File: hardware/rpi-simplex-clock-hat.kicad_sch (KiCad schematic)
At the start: 19 parts, among them J1 TBP01R1-508-04BE, J2 Barrel_Jack_Switch, J3 GPIO, U1 LAA120, U2 CAT24C256

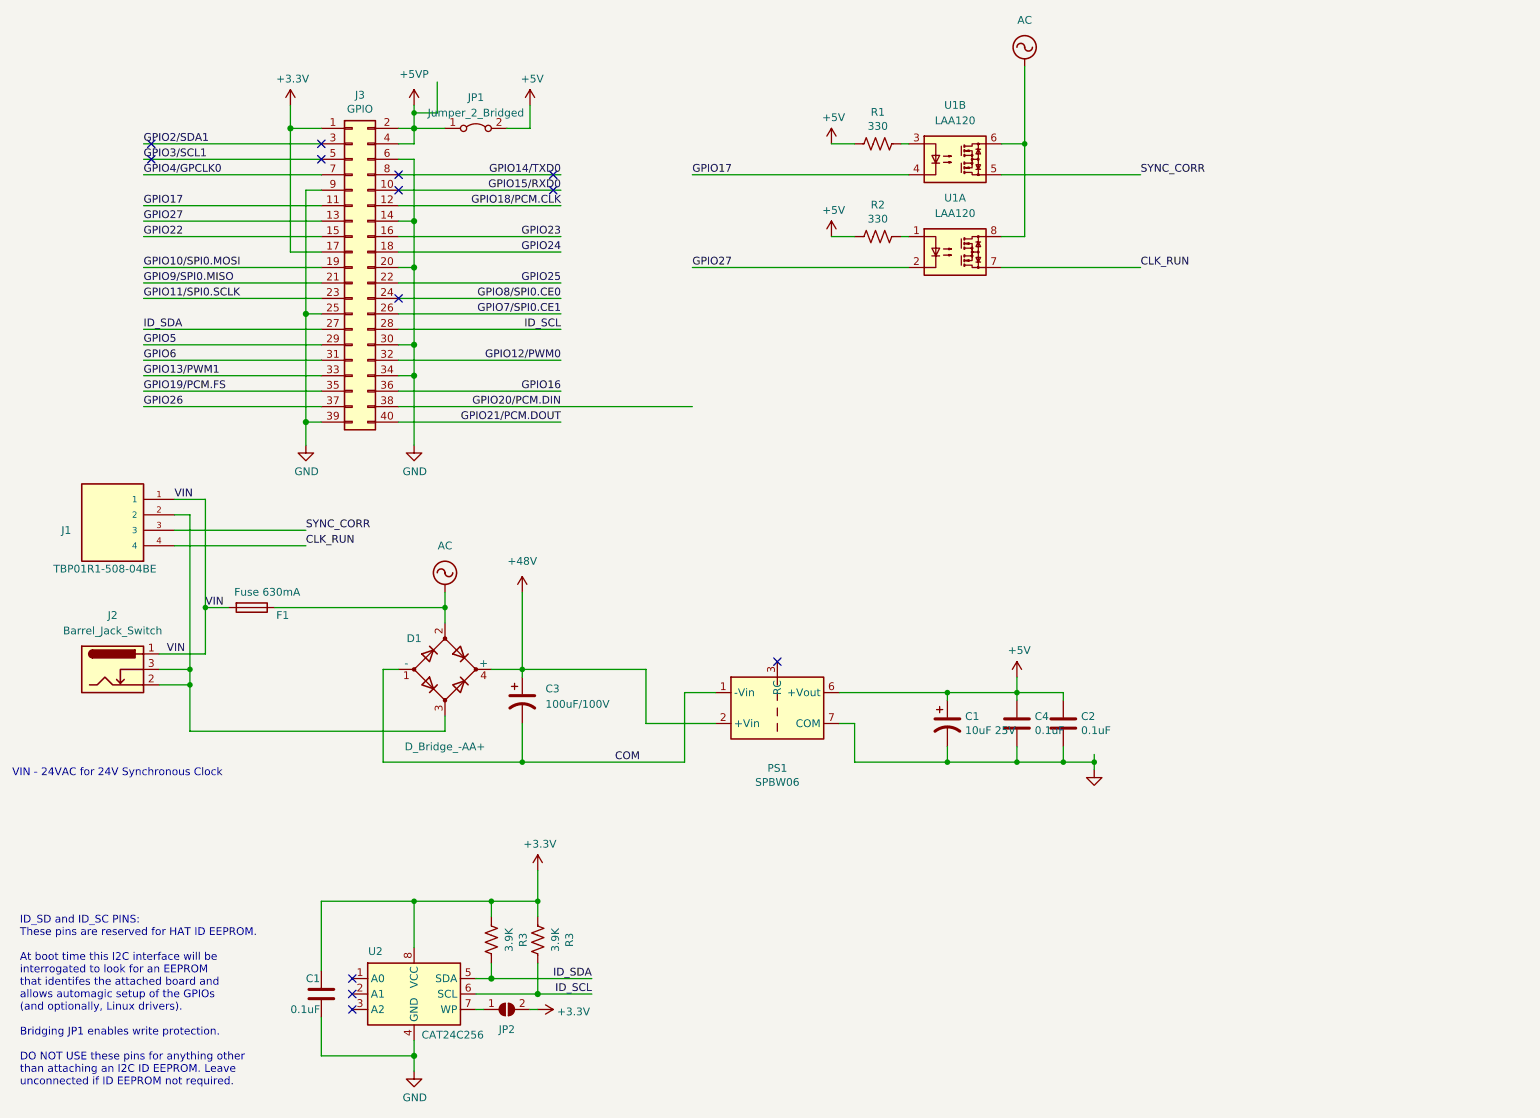
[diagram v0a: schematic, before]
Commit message: Rev 1: Fix minor issues in Rev 0.
1. Turn SSRs on with logic 1 to GPIO outputs.  This is needed so that
   the SSRs don't become enabled when the GPIO17 and GPIO27 are set to
   outputs.  These GPIOs are pulled low.

2. Add alternate footprint location (J4) for AC input barrel jack.

3. Add additional mounting holes for Raspberry Pi Zero / Zero 2 W.

4. Correct pinout for the bridge rectifier D1.
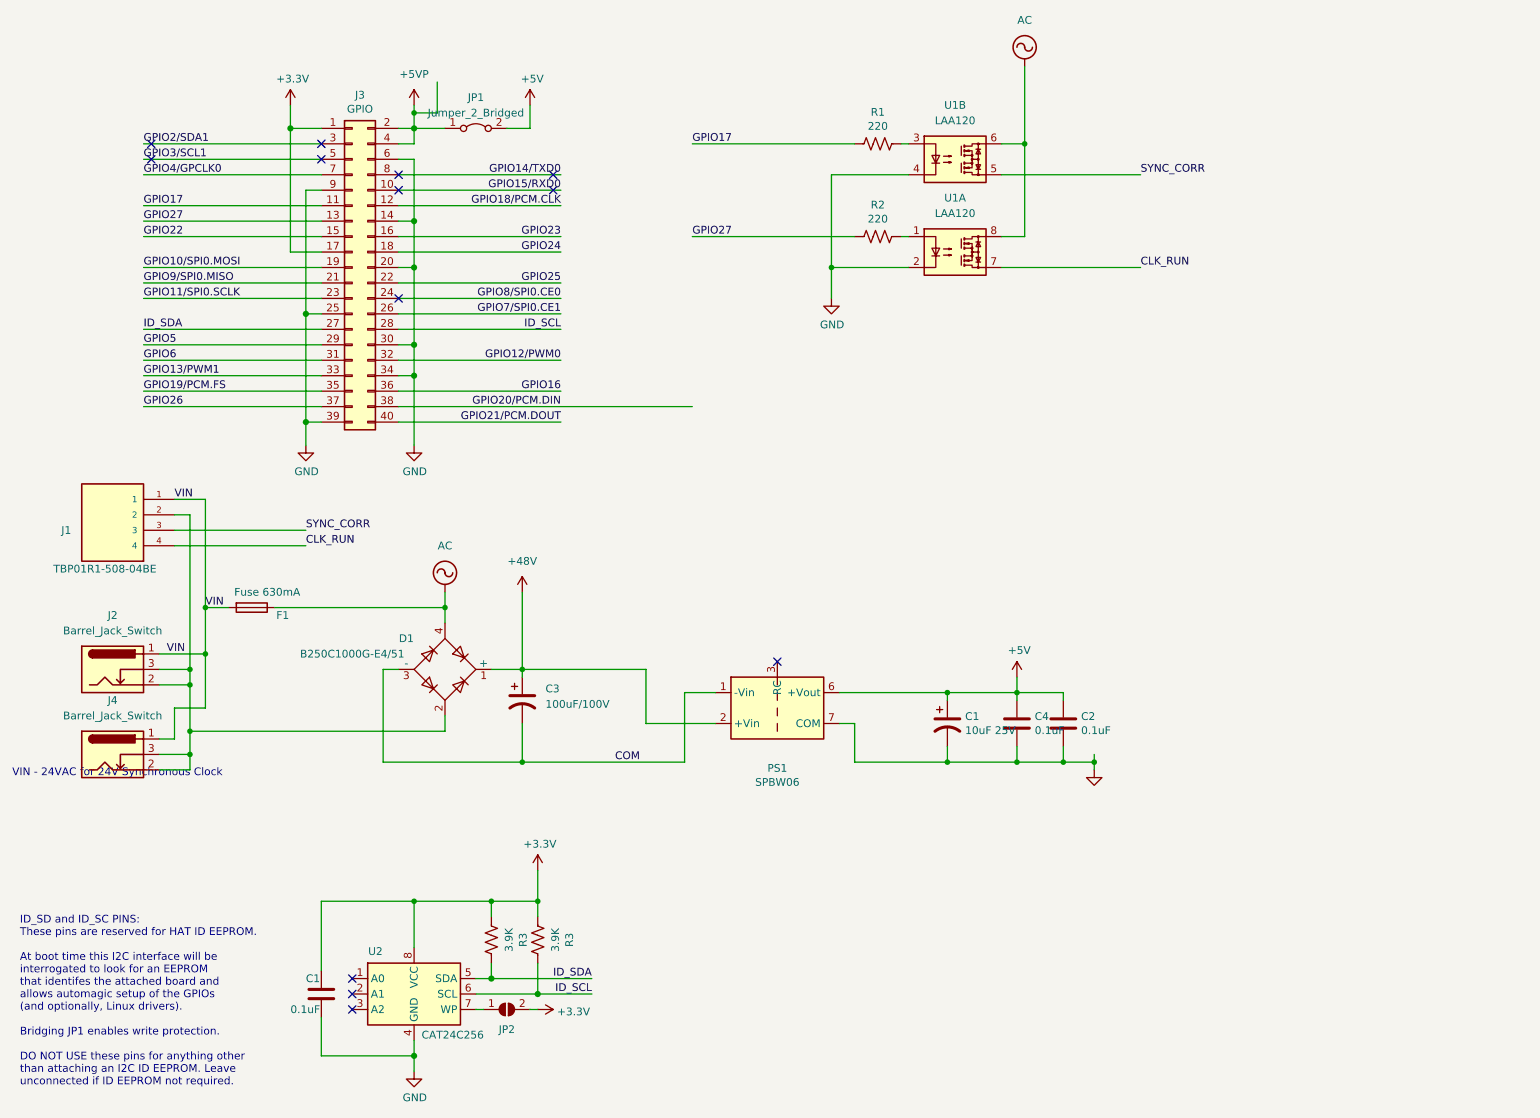
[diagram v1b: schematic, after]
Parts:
- removed D1: D_Bridge_-AA+, Diode_THT:Diode_Bridge_Round_D8.9mm, symbol Device:D_Bridge_-AA+
- added D1: B250C1000G-E4/51, Diode_THT:Diode_Bridge_Round_D9.8mm, symbol Diode_Bridge:B250C1500G
- added J4: Barrel_Jack_Switch, Connector_BarrelJack:BarrelJack_Horizontal, symbol Connector:Barrel_Jack_Switch
- R1, R2: value 330 -> 220
- R3: footprint Resistor_THT:R_Axial_DIN0207_L6.3mm_D2.5mm_P7.62mm_Horizontal -> Resistor_THT:R_Axial_DIN0207_L6.3mm_D2.5mm_P2.54mm_Vertical
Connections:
- net +48V: now also D1.1 (+)
- net +5V: no longer R1.2, R2.2
- net AC: now also D1.4
- net COM: now also D1.3 (-)
- net GND: now also U1.2, U1.4
- net GPIO17: now also R1.2; no longer U1.4
- net GPIO27: now also R2.2; no longer U1.2
- net VIN: now also J4.1
- net at J1.2, J2.2, J2.3: now also D1.2, J4.2, J4.3

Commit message: Update for KiCAD 8.0
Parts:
- added MH1, MH2, MH3, MH4, MH5, MH6: MountingHole_2.7mm_M2.5, MountingHole:MountingHole_2.7mm_M2.5, symbol Mechanical:MountingHole
- U1: value LAA120 -> LAA108

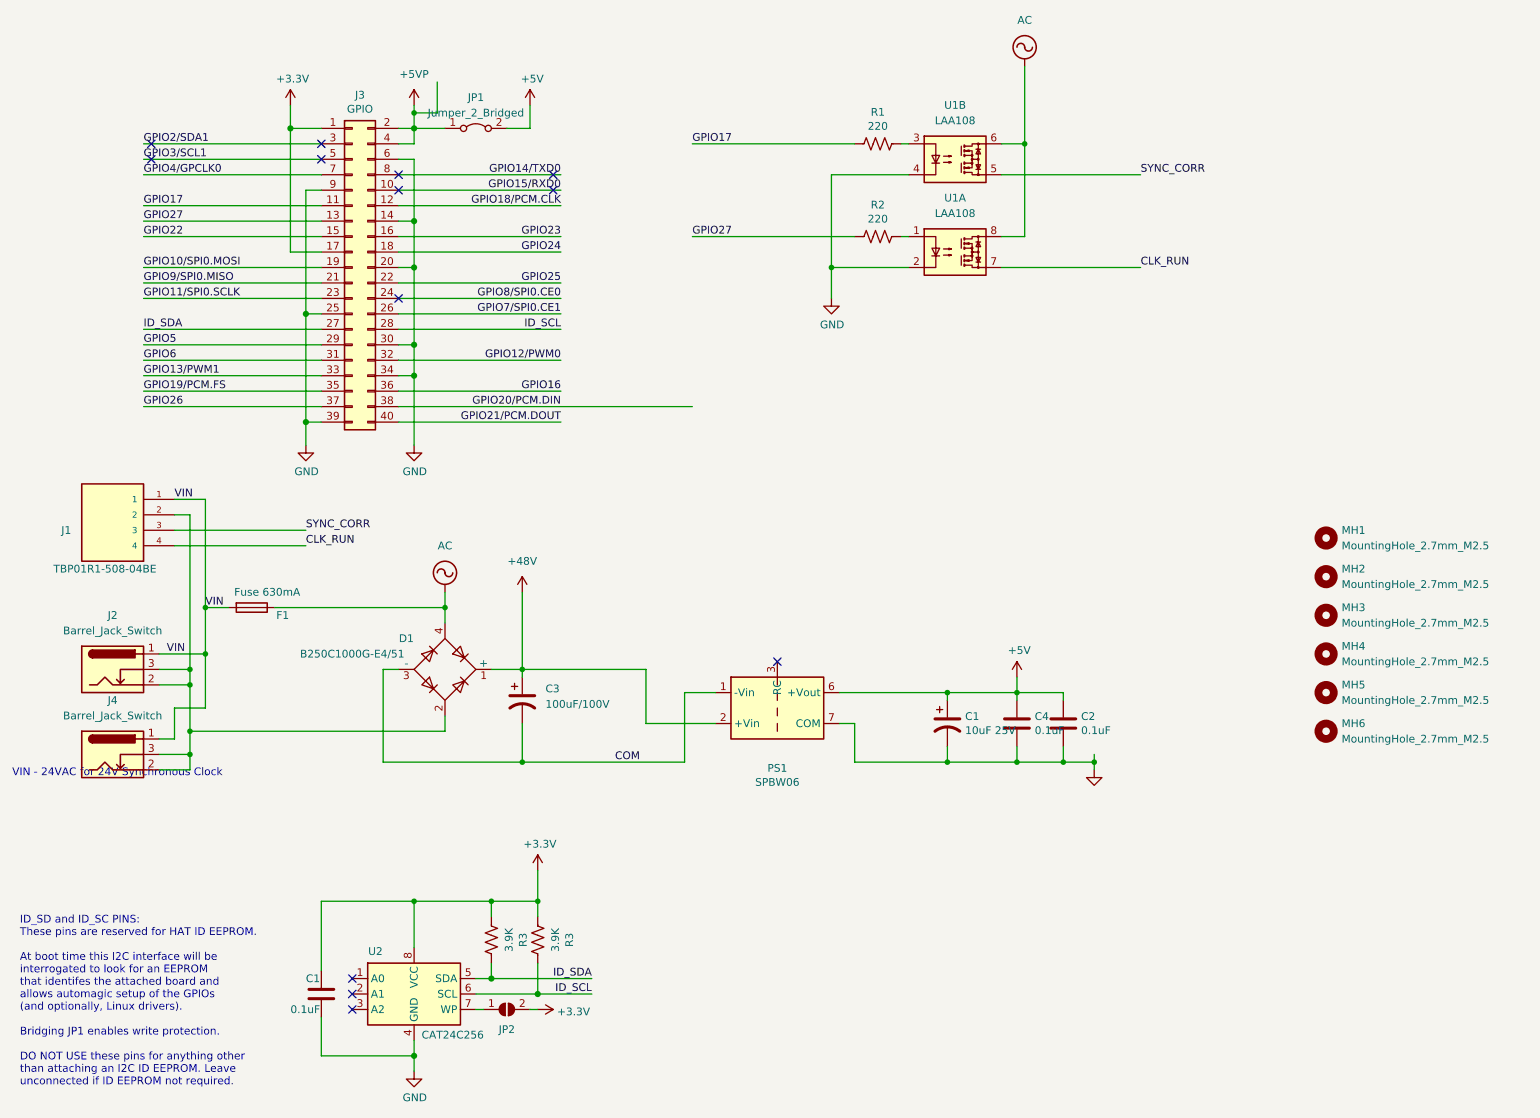
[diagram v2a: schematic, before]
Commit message: Add interactive BOM, update to KiCAD 8.0.1.
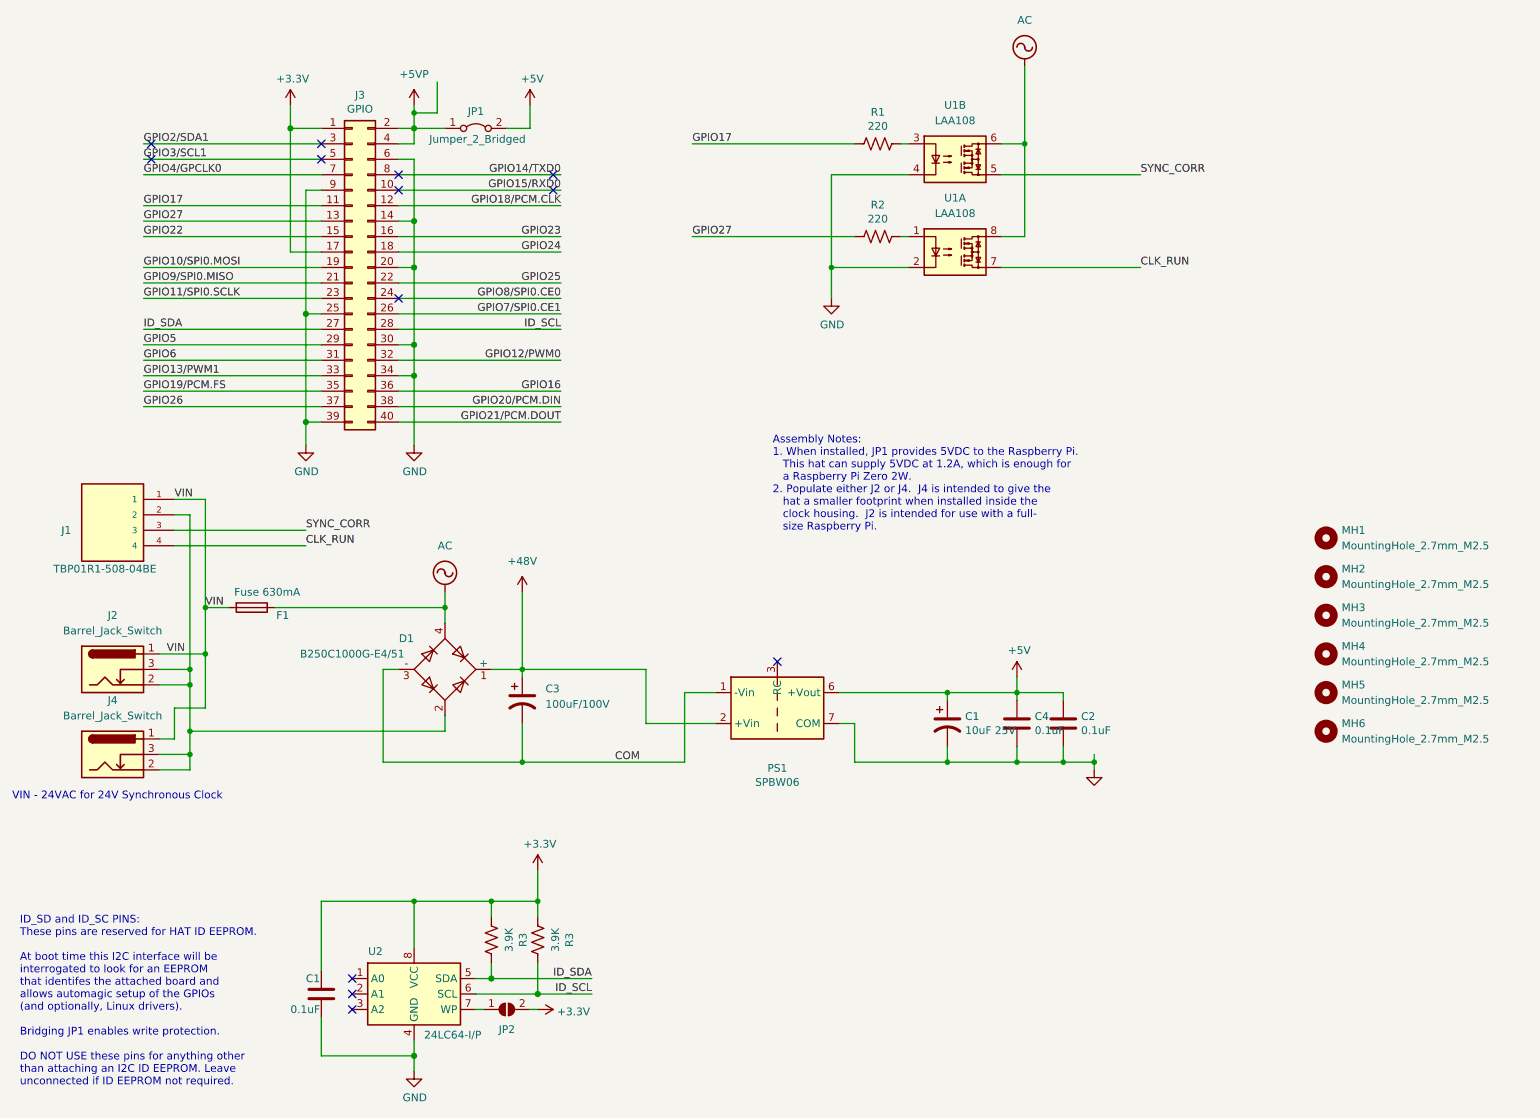
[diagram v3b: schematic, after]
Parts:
- C1, C2, C4: MPN (none) -> C315C104M5U5TA7303
- C1: MPN (none) -> ECE-A1EN100UI
- C3: MPN (none) -> REF1016101M100K; Note (none) -> Choose a capacitor 16mm tall or less, to provide clearance 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
- D1: MPN (none) -> B250C1000G-E4/51
- F1: MPN (none) -> 0251.630MAT1L
- J1: MPN (none) -> TBP01R1-508-04BE
- J2: MPN (none) -> RAPC722BK; Note (none) -> Populate either J2 or J4. J4 is intended to give the hat a 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
- J3: MPN (none) -> SSQ-120-01-F-D; Note (none) -> Mount on bottom of PCB.
- J4: MPN (none) -> RAPC722BK
- JP1: Note (none) -> When installed, JP1 provides 5VDC to the Raspberry Pi. This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
- PS1: MPN (none) -> SPBW06F-05
- R1, R2: MPN (none) -> CFM12JT220R
- R3: MPN (none) -> CFM12JT3K90
- U1: MPN (none) -> LAA108
- U2: value CAT24C256 -> 24LC64-I/P; MPN (none) -> 24LC64-I/P
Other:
- note added: "Assembly Notes: 1. When installed, JP1 provides 5VDC to the Raspberry Pi. This hat can supply 5VDC at 1.2A, which is enough for a Raspberry Pi Zero 2W. 2. Populate either J2 or J4. J4 is intended to give the hat a smaller footprint when installed inside the clock housing. J2 is intended for use with a full- size Raspberry Pi."
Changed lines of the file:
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@@
 	(wire
 		(pts
+			(xy 78.74 81.28) (xy 105.41 81.28)
+		)
+		(stroke
+			(width 0)
+			(type default)
+		)
+	)
+	(wire
+		(pts
 			(xy 119.38 124.46) (xy 119.38 133.35)
 		)
@@
 	(wire
 		(pts
-			(xy 78.74 81.28) (xy 127 81.28)
-		)
-		(stroke
-			(width 0)
-			(type solid)
-		)
-	)
-	(wire
-		(pts
 			(xy 93.98 172.72) (xy 93.98 175.26)
 		)
@@
 	(text "VIN - 24VAC for 24V Synchronous Clock\n"
 		(exclude_from_sim no)
-		(at 15.24 142.24 0)
+		(at 15.24 146.05 0)
 		(effects
 			(font
@@
 		)
 	)
+	(text "Assembly Notes:\n1. When installed, JP1 provides 5VDC to the Raspberry Pi.\n   This hat can supply 5VDC at 1.2A, which is enough for\n   a Raspberry Pi Zero 2W.\n2. Populate either J2 or J4.  J4 is intended to give the\n   hat a smaller footprint when installed inside the\n   clock housing.  J2 is intended for use with a full-\n   size Raspberry Pi."
+		(exclude_from_sim no)
+		(at 140.208 93.98 0)
+		(effects
+			(font
+				(size 1.27 1.27)
+			)
+			(justify left)
+		)
+	)
 	(text "ID_SD and ID_SC PINS:\nThese pins are reserved for HAT ID EEPROM.\n\nAt boot time this I2C interface will be\ninterrogated to look for an EEPROM\nthat identifes the attached board and\nallows automagic setup of the GPIOs\n(and optionally, Linux drivers).\n\nBridging JP1 enables write protection.\n\nDO NOT USE these pins for anything other\nthan attaching an I2C ID EEPROM. Leave\nunconnected if ID EEPROM not required."
 		(exclude_from_sim no)
@@
 			)
 		)
+		(property "MPN" "SSQ-120-01-F-D"
+			(at 71.12 58.42 0)
+			(effects
+				(font
+					(size 1.27 1.27)
+				)
+				(hide yes)
+			)
+		)
+		(property "Note" "Mount on bottom of PCB."
+			(at 71.12 58.42 0)
+			(effects
+				(font
+					(size 1.27 1.27)
+				)
+				(hide yes)
+			)
+		)
 		(pin "1"
 		)
@@
 			)
 		)
+		(property "MPN" "RAPC722BK"
+			(at 31.75 124.46 0)
+			(effects
+				(font
+					(size 1.27 1.27)
+				)
+				(hide yes)
+			)
+		)
+		(property "Note" "Populate either J2 or J4.  J4 is intended to give the hat a smaller footprint when installed inside the clock housing.  J2 is intended for use with a full-size Raspberry Pi."
+			(at 31.75 124.46 0)
+			(effects
+				(font
+					(size 1.27 1.27)
+				)
+				(hide yes)
+			)
+		)
 		(pin "3"
 		)
@@
 			)
 		)
+		(property "MPN" "TBP01R1-508-04BE"
+			(at 31.75 101.6 0)
+			(effects
+				(font
+					(size 1.27 1.27)
+				)
+				(hide yes)
+			)
+		)
 		(pin "1"
 		)
@@
 			)
 		)
+		(property "MPN" "SPBW06F-05"
+			(at 140.97 130.81 0)
+			(effects
+				(font
+					(size 1.27 1.27)
+				)
+				(hide yes)
+			)
+		)
 		(pin "1"
 		)
@@
 			)
 		)
+		(property "MPN" "C315C104M5U5TA7303"
+			(at 66.04 177.8 0)
+			(effects
+				(font
+					(size 1.27 1.27)
+				)
+				(hide yes)
+			)
+		)
 		(pin "1"
 		)
@@
 			)
 		)
+		(property "MPN" "CFM12JT220R"
+			(at 157.48 38.1 90)
+			(effects
+				(font
+					(size 1.27 1.27)
+				)
+				(hide yes)
+			)
+		)
 		(pin "1"
 		)
@@
 			)
 		)
-		(property "Value" "CAT24C256"
+		(property "Value" "24LC64-I/P"
 			(at 87.63 184.5245 0)
 			(effects
@@
 			)
 		)
+		(property "MPN" "24LC64-I/P"
+			(at 81.28 177.8 0)
+			(effects
+				(font
+					(size 1.27 1.27)
+				)
+				(hide yes)
+			)
+		)
 		(pin "1"
 		)
@@
 			)
 		)
+		(property "MPN" "CFM12JT220R"
+			(at 157.48 53.34 90)
+			(effects
+				(font
+					(size 1.27 1.27)
+				)
+				(hide yes)
+			)
+		)
 		(pin "1"
 		)
@@
 		(on_board yes)
 		(dnp no)
-		(fields_autoplaced yes)
 		(property "Reference" "JP1"
-			(at 91.44 30.48 0)
+			(at 91.44 32.766 0)
 			(effects
 				(font
@@
 		)
 		(property "Value" "Jumper_2_Bridged"
-			(at 91.44 33.02 0)
+			(at 91.694 37.338 0)
 			(effects
 				(font
@@
 			)
 		)
+		(property "Note" "When installed, JP1 provides 5VDC to the Raspberry Pi.  This hat can supply 5VDC at 1.2A, which is enough for a Raspberry Pi Zero 2W."
+			(at 91.44 35.56 0)
+			(effects
+				(font
+					(size 1.27 1.27)
+				)
+				(hide yes)
+			)
+		)
 		(pin "2"
 		)
@@
 			)
 		)
+		(property "MPN" "B250C1000G-E4/51"
+			(at 86.36 124.46 0)
+			(effects
+				(font
+					(size 1.27 1.27)
+				)
+				(hide yes)
+			)
+		)
 		(pin "2"
 		)
@@
 			)
 		)
+		(property "MPN" "CFM12JT3K90"
+			(at 101.6 168.91 90)
+			(effects
+				(font
+					(size 1.27 1.27)
+				)
+				(hide yes)
+			)
+		)
 		(pin "1"
 		)
@@
 			)
 		)
+		(property "MPN" "C315C104M5U5TA7303"
+			(at 180.34 133.35 0)
+			(effects
+				(font
+					(size 1.27 1.27)
+				)
+				(hide yes)
+			)
+		)
 		(pin "1"
 		)
@@
 			)
 		)
+		(property "MPN" "REF1016101M100K"
+			(at 99.06 129.54 0)
+			(effects
+				(font
+					(size 1.27 1.27)
+				)
+				(hide yes)
+			)
+		)
+		(property "Note" "Choose a capacitor 16mm tall or less, to provide clearance inside the clock movement cover."
+			(at 99.06 129.54 0)
+			(effects
+				(font
+					(size 1.27 1.27)
+				)
+				(hide yes)
+			)
+		)
 		(pin "1"
 		)
@@
 			)
 		)
+		(property "MPN" "ECE-A1EN100UI"
+			(at 168.91 133.35 0)
+			(effects
+				(font
+					(size 1.27 1.27)
+				)
+				(hide yes)
+			)
+		)
 		(pin "1"
 		)
@@
 			)
 		)
+		(property "MPN" "CFM12JT3K90"
+			(at 93.98 168.91 90)
+			(effects
+				(font
+					(size 1.27 1.27)
+				)
+				(hide yes)
+			)
+		)
 		(pin "1"
 		)
@@
 			)
 		)
+		(property "MPN" "0251.630MAT1L"
+			(at 54.61 114.3 90)
+			(effects
+				(font
+					(size 1.27 1.27)
+				)
+				(hide yes)
+			)
+		)
 		(pin "1"
 		)
@@
 			)
 		)
+		(property "MPN" "RAPC722BK"
+			(at 31.75 138.43 0)
+			(effects
+				(font
+					(size 1.27 1.27)
+				)
+				(hide yes)
+			)
+		)
+		(property "Note" ""
+			(at 31.75 138.43 0)
+			(effects
+				(font
+					(size 1.27 1.27)
+				)
+				(hide yes)
+			)
+		)
 		(pin "3"
 		)
@@
 			)
 		)
+		(property "MPN" "LAA108"
+			(at 170.18 40.64 0)
+			(effects
+				(font
+					(size 1.27 1.27)
+				)
+				(hide yes)
+			)
+		)
 		(pin "5"
 		)
@@
 			)
 		)
+		(property "MPN" "LAA108"
+			(at 170.18 55.88 0)
+			(effects
+				(font
+					(size 1.27 1.27)
+				)
+				(hide yes)
+			)
+		)
 		(pin "5"
 		)
@@
 			(at 187.96 133.35 0)
 			(effects
+				(font
+					(size 1.27 1.27)
+				)
+				(hide yes)
+			)
+		)
+		(property "MPN" "C315C104M5U5TA7303"
+			(at 187.96 133.35 0)
+			(effects
